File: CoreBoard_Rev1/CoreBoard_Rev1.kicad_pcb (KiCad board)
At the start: 2 copper layers, 135.1 x 84.3 mm, 91 parts, among them J1 RJ45_LED_Shielded, SW1 SW_Push, SW10 SW_Push, SW11 SW_Push, SW12 SW_Push, SW13 SW_Push, SW14 SW_Push, SW15 SW_Push, SW16 SW_SPDT, SW2 SW_Push, SW3 SW_Push, SW4 SW_Push, SW5 SW_Push, SW6 SW_Push, SW7 SW_Push, SW8 SW_Push, SW9 SW_Push, U1 Teensy4.1_DEV-16771, U2 TSR_1-2450, U4 74HC148, U5 74HC148, U6 74HC00, U7 OKI

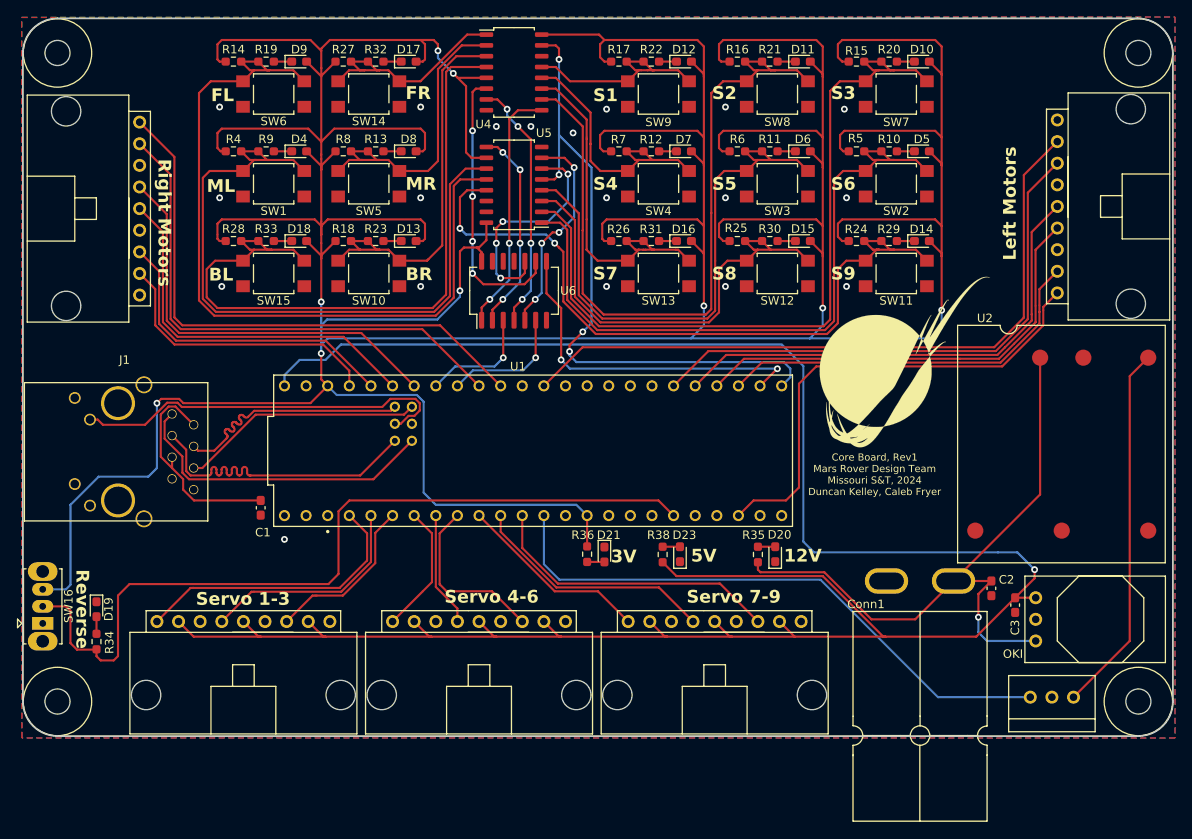
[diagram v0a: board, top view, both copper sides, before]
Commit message: Changes to Labels
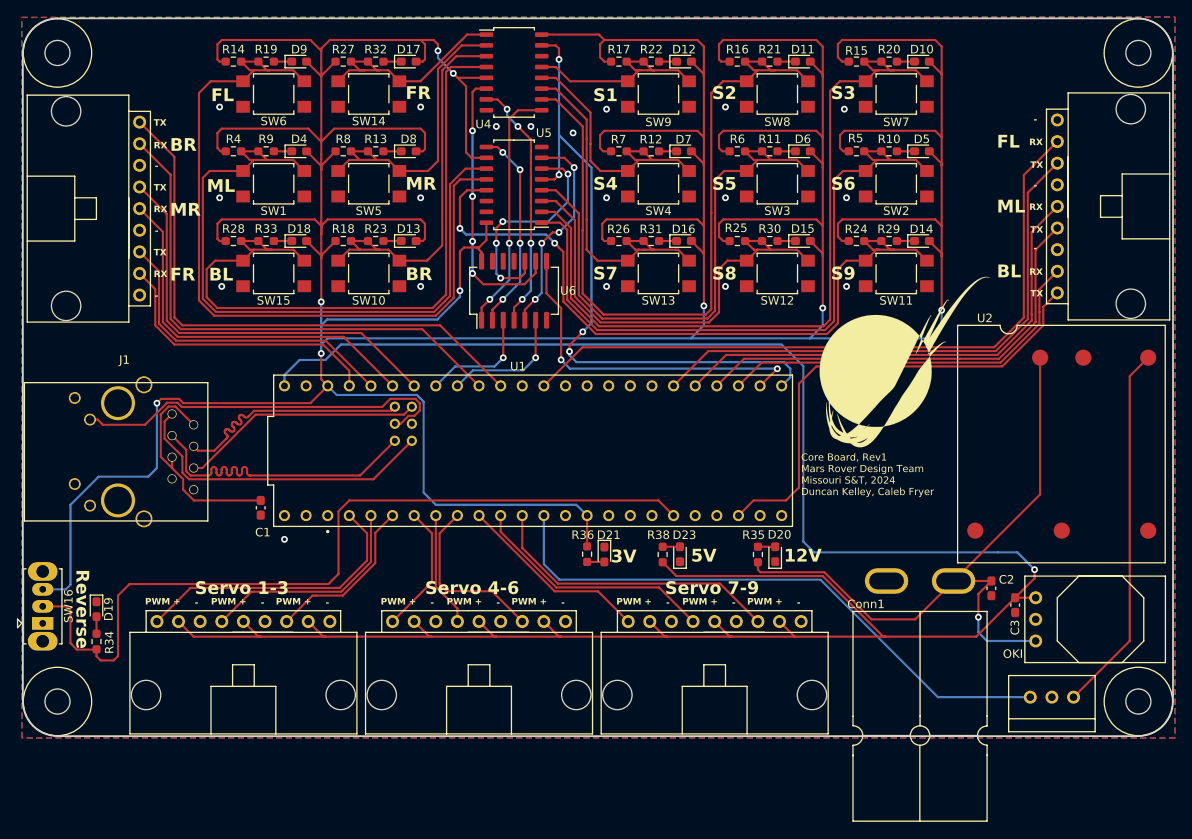
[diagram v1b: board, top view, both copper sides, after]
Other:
- board text added: "+"
- board text added: "-"
- board text added: "PWM"
- board text added: "RX"
- board text added: "TX"
- board text removed: "Left Motors"
- board text removed: "Right Motors"

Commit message: updating button traces
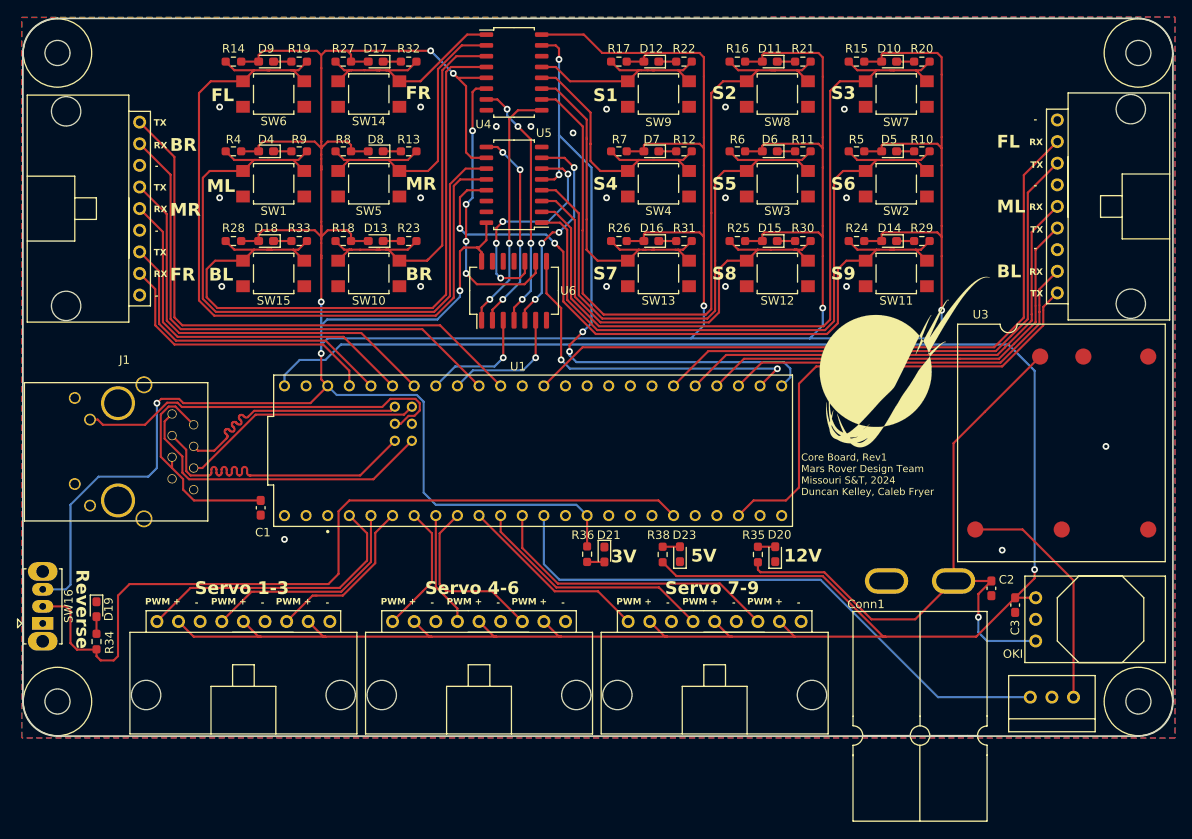
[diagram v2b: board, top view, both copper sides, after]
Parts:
- removed U2: TSR_1-2450, MRDT_Devices:SHHD003A0A-SRZ
- added U3: SHHD003A0A, MRDT_Devices:SHHD003A0A-SRZ, F.Cu at (176.6, 68.2)
- moved D11 3.89 mm to (154.6, 37.3), turned to 180 degrees
- moved D15 3.89 mm to (154.6, 58.4), turned to 180 degrees
- moved D18 3.89 mm to (95.4, 58.4), turned to 180 degrees
- moved D4 3.89 mm to (95.4, 47.9), turned to 180 degrees
- moved D6 3.89 mm to (154.6, 47.9), turned to 180 degrees
- moved D9 3.89 mm to (95.4, 37.3), turned to 180 degrees
- moved R11 3.89 mm to (158.4, 47.9), turned to 180 degrees
- moved R19 3.89 mm to (99.3, 37.3), turned to 180 degrees
- moved R21 3.89 mm to (158.4, 37.3), turned to 180 degrees
- moved R30 3.89 mm to (158.4, 58.4), turned to 180 degrees
- moved R33 3.89 mm to (99.3, 58.4), turned to 180 degrees
- moved R9 3.89 mm to (99.3, 47.9), turned to 180 degrees
- moved D13 3.87 mm to (108.3, 58.4), turned to 180 degrees
- moved D17 3.87 mm to (108.3, 37.3), turned to 180 degrees
- moved D8 3.87 mm to (108.3, 47.9), turned to 180 degrees
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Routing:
- net +3V3: track 650.7 -> 531.9 mm
- net Net-(U3-Vout+): track 43.5 -> 27.7 mm
- net +5V: track 273.2 -> 275.2 mm
- net B14: track 45.9 -> 47.3 mm
- net Net-(U4-S2): track 33.0 -> 34.1 mm
- net B12: track 26.5 -> 27.4 mm
- net B10: track 31.8 -> 32.5 mm
- net B6: track 54.8 -> 55.5 mm
- net B13: track 36.5 -> 37.1 mm
- net GND: vias 19 -> 21

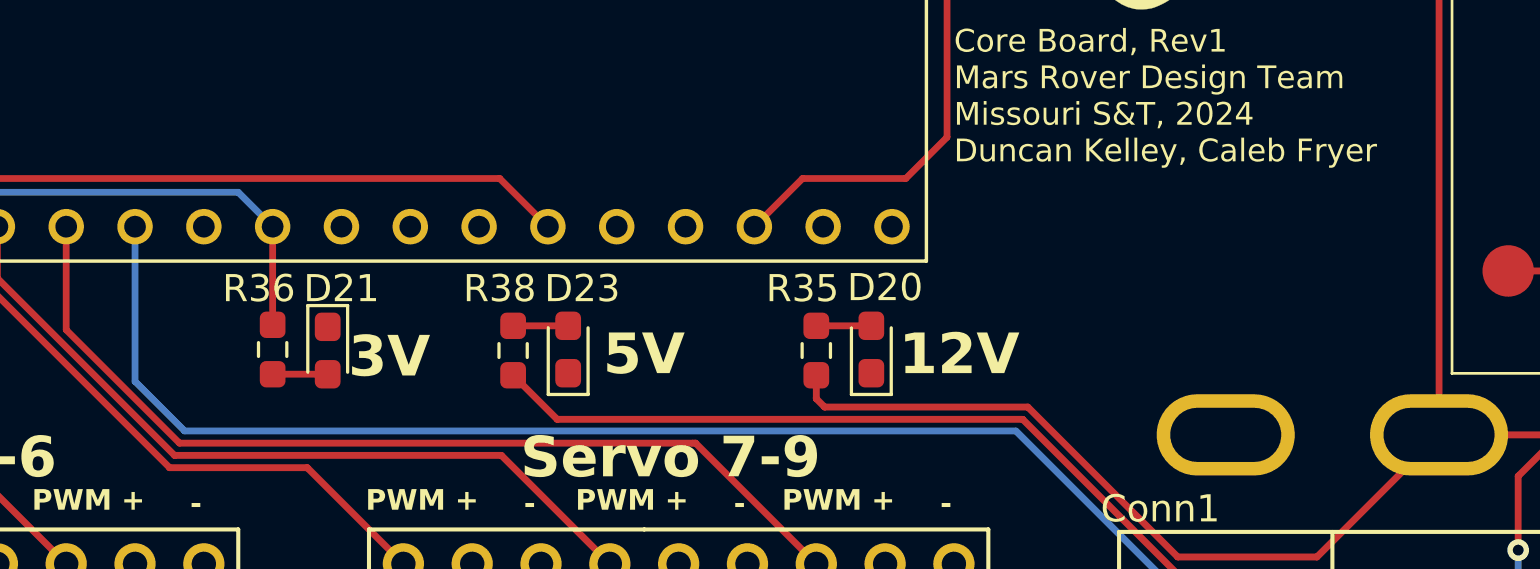
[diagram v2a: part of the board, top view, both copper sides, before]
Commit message: Signatures Added
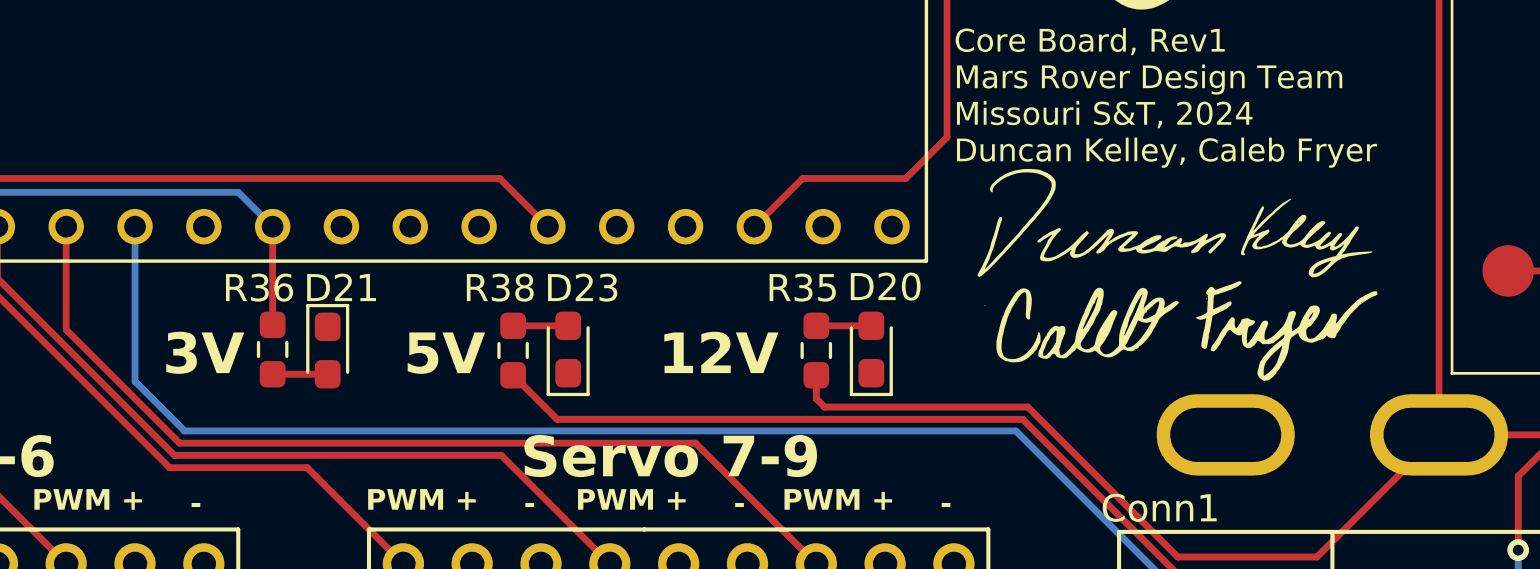
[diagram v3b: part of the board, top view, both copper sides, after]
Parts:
- added G***: LOGO, Signatures:MRDT_CalebSig_15mmx5.4mm, F.Cu at (166.5, 93.8)
- added G***: LOGO, Signatures:MRDT_DuncanSig_15mmx4.9mm, F.Cu at (166.4, 90.6)

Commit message: Layout Changes
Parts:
- moved U3 0.08 mm to (176.6, 68.3)
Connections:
- U3 pad 3: unconnected-(U3-On/OFF-Pad3) -> GND
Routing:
- net GND: vias 21 -> 30
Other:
- board text added: "PV"
- board text removed: "12V"
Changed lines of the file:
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@@
   (net 98 "unconnected-(U1-MISO-Pad12)")
   (net 99 "Net-(U3-Vout+)")
-  (net 100 "unconnected-(U3-On{slash}OFF-Pad3)")
-  (net 101 "unconnected-(U3-TRIM-Pad5)")
+  (net 100 "unconnected-(U3-TRIM-Pad5)")
   (footprint "LED_SMD:LED_0603_1608Metric_Pad1.05x0.95mm_HandSolder" (layer "F.Cu")
     (at 154.559 47.879 180)
@@
   )
   (footprint "MRDT_Devices:SHHD003A0A-SRZ" (layer "F.Cu")
-    (at 176.622 68.192 -90)
+    (at 176.622 68.2682 -90)
     (property "Sheetfile" "CoreBoard_Rev1.kicad_sch")
     (property "Sheetname" "")
@@
       (net 1 "GND") (pinfunction "Vin-") (pintype "input"))
     (pad "3" smd circle (at 3.8 -22.4 270) (size 1.9 1.9) (layers "F.Cu" "F.Paste" "F.Mask")
-      (net 100 "unconnected-(U3-On{slash}OFF-Pad3)") (pinfunction "On/OFF") (pintype "input+no_connect"))
+      (net 1 "GND") (pinfunction "On/OFF") (pintype "input"))
     (pad "4" smd circle (at 24.12 -22.4 270) (size 1.9 1.9) (layers "F.Cu" "F.Paste" "F.Mask")
       (net 1 "GND") (pinfunction "Vout-") (pintype "output"))
     (pad "5" smd circle (at 24.12 -12.24 270) (size 1.9 1.9) (layers "F.Cu" "F.Paste" "F.Mask")
-      (net 101 "unconnected-(U3-TRIM-Pad5)") (pinfunction "TRIM") (pintype "output+no_connect"))
+      (net 100 "unconnected-(U3-TRIM-Pad5)") (pinfunction "TRIM") (pintype "output+no_connect"))
     (pad "6" smd circle (at 24.12 -2.08 270) (size 1.9 1.9) (layers "F.Cu" "F.Paste" "F.Mask")
       (net 99 "Net-(U3-Vout+)") (pinfunction "Vout+") (pintype "output"))
@@
     (effects (font (size 0.762 0.762) (thickness 0.1905) bold) (justify left bottom))
   )
-  (gr_text "12V" (at 147.32 96.266) (layer "F.SilkS")
+  (gr_text "PV" (at 148.844 96.266) (layer "F.SilkS")
     (effects (font (size 1.5 1.5) (thickness 0.3) bold) (justify left bottom))
   )
@@
   (via (at 113.538 53.34) (size 0.8) (drill 0.4) (layers "F.Cu" "B.Cu") (free) (net 1))
   (via (at 181.864 94.742) (size 0.8) (drill 0.4) (layers "F.Cu" "B.Cu") (free) (net 1))
+  (via (at 89.662 87.63) (size 0.8) (drill 0.4) (layers "F.Cu" "B.Cu") (free) (net 1))
   (via (at 149.352 63.754) (size 0.8) (drill 0.4) (layers "F.Cu" "B.Cu") (free) (net 1))
+  (via (at 176.403 107.442) (size 0.8) (drill 0.4) (layers "F.Cu" "B.Cu") (free) (net 1))
+  (via (at 97.282 82.042) (size 0.8) (drill 0.4) (layers "F.Cu" "B.Cu") (free) (net 1))
   (via (at 149.352 53.34) (size 0.8) (drill 0.4) (layers "F.Cu" "B.Cu") (free) (net 1))
   (via (at 149.352 42.672) (size 0.8) (drill 0.4) (layers "F.Cu" "B.Cu") (free) (net 1))
   (via (at 131.445 45.72) (size 0.8) (drill 0.4) (layers "F.Cu" "B.Cu") (free) (net 1))
+  (via (at 131.191 68.199) (size 0.8) (drill 0.4) (layers "F.Cu" "B.Cu") (free) (net 1))
   (via (at 89.916 53.34) (size 0.8) (drill 0.4) (layers "F.Cu" "B.Cu") (free) (net 1))
   (via (at 163.576 63.754) (size 0.8) (drill 0.4) (layers "F.Cu" "B.Cu") (free) (net 1))
   (via (at 163.576 53.34) (size 0.8) (drill 0.4) (layers "F.Cu" "B.Cu") (free) (net 1))
+  (via (at 78.74 83.439) (size 0.8) (drill 0.4) (layers "F.Cu" "B.Cu") (free) (net 1))
   (via (at 113.538 63.754) (size 0.8) (drill 0.4) (layers "F.Cu" "B.Cu") (free) (net 1))
   (via (at 113.538 42.672) (size 0.8) (drill 0.4) (layers "F.Cu" "B.Cu") (free) (net 1))
   (via (at 163.322 42.926) (size 0.8) (drill 0.4) (layers "F.Cu" "B.Cu") (free) (net 1))
+  (via (at 105.41 94.361) (size 0.8) (drill 0.4) (layers "F.Cu" "B.Cu") (free) (net 1))
   (via (at 194.056 82.55) (size 0.8) (drill 0.4) (layers "F.Cu" "B.Cu") (free) (net 1))
   (via (at 135.382 53.34) (size 0.8) (drill 0.4) (layers "F.Cu" "B.Cu") (free) (net 1))
@@
   (via (at 97.536 93.472) (size 0.8) (drill 0.4) (layers "F.Cu" "B.Cu") (free) (net 1))
   (via (at 90.17 63.754) (size 0.8) (drill 0.4) (layers "F.Cu" "B.Cu") (free) (net 1))
+  (via (at 69.723 93.345) (size 0.8) (drill 0.4) (layers "F.Cu" "B.Cu") (free) (net 1))
   (via (at 89.916 42.672) (size 0.8) (drill 0.4) (layers "F.Cu" "B.Cu") (free) (net 1))
+  (via (at 75.438 93.345) (size 0.8) (drill 0.4) (layers "F.Cu" "B.Cu") (free) (net 1))
   (via (at 126.492 44.958) (size 0.8) (drill 0.4) (layers "F.Cu" "B.Cu") (free) (net 1))
+  (via (at 89.281 80.01) (size 0.8) (drill 0.4) (layers "F.Cu" "B.Cu") (free) (net 1))
   (segment (start 83.003 83.765) (end 84.328 85.09) (width 0.25) (layer "F.Cu") (net 2))
   (segment (start 86.900563 88.9) (end 85.630563 87.63) (width 0.25) (layer "F.Cu") (net 2))
